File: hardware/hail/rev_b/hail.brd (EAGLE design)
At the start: 20.3 x 36.6 mm, 77 parts, among them J1 MICRO_USB_B_HIROSE_ZX62R-B-5P, J2 TC2030-JLINK-NL_NOSILK, J3 TC2030-JLINK-NL_NOSILK, U1 FT231XQ, U2 FXOS8700CQ, U3 ISL29035, U4 MAX8887EZK33+T, U5 NRF51822QF, U6 SAM4LC8BA, U7 SI7021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

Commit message: Hail rev B!
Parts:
- removed JP3: M12PTH-CST-L, Particle:1X12-CASTELLATED
- removed JP4: M12PTH-CST-R, Particle:1X12-CASTELLATED
- removed U$4: (no value), logos:HAIL
- added J4, J5: TC2030-JLINK-NL_NOSILK, connector:TC2030-IDC-NL_NOSILK
- J2: value TC2030-JLINK-NL_NOSILK -> M12PTH-CST-L; device connector:TC2030-IDC-NL_NOSILK -> Particle:1X12-CASTELLATED
- J3: value TC2030-JLINK-NL_NOSILK -> M12PTH-CST-R; device connector:TC2030-IDC-NL_NOSILK -> Particle:1X12-CASTELLATED
- R10: value 100k -> 10k
- R13: value 1k -> 100k
- R6: value 10k -> 1k
- U$3: device logos:UMICH_SOLID_75MIL -> logos:LAB11_SOLID_80MIL
- moved R12 23.6 mm to (7.72, 10.9), turned to 90 degrees
- moved J3 18.2 mm to (19.1, 18.3), flipped to the top, turned to 0 degrees
- moved R10 14.6 mm to (13.3, 24.0), turned to 270 degrees
- moved R9 13.2 mm to (4.50, 14.2), turned to 0 degrees
- moved J2 11.8 mm to (1.27, 18.3), turned to 180 degrees
- moved R8 11.8 mm to (2.79, 25.9)
- moved R6 11.0 mm to (10.2, 25.6), turned to 0 degrees
- moved R13 9.71 mm to (16.8, 32.8), turned to 270 degrees
- moved R7 9.33 mm to (3.81, 16.6), turned to 90 degrees
- moved R11 1.02 mm to (6.71, 10.9)
- moved U$3 0.41 mm to (8.13, 23.1)
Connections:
- net !LIGHT_INT: now also R9.1; no longer R8.1
- net !NRF_RESET: now also J5.2; no longer J3.2
- net !SAM4L_RESET: now also J3.11, J4.3, R6.2; no longer J2.3, JP4.11, R13.2
- net 5V: now also J2.1; no longer JP3.1
- net BUCK/LDO_N1: now also R10.2; no longer R9.2
- net BUTTON: now also R13.1; no longer R12.1
- net GND: now also J2.2, J3.9, J4.5, J5.5, R10.1; no longer J2.5, J3.5, JP3.2, JP4.9, R9.1
- net N$24: now also R6.1; no longer R13.1
- net N$6: now also J5.4; no longer J3.4
- net PARTICLE_A0: now also J2.12; no longer JP3.12
- net PARTICLE_A1: now also J2.11; no longer JP3.11
- net PARTICLE_A2: now also J2.10; no longer JP3.10
- net PARTICLE_A3: now also J2.9; no longer JP3.9
- net PARTICLE_A4: now also J2.8; no longer JP3.8
- net PARTICLE_A5: now also J2.7; no longer JP3.7
- net PARTICLE_D0: now also J3.1; no longer JP4.1
- net PARTICLE_D1: now also J3.2; no longer JP4.2
- net PARTICLE_D2: now also J3.3; no longer JP4.3
- net PARTICLE_D3: now also J3.4; no longer JP4.4
- net PARTICLE_D4: now also J3.5; no longer JP4.5
- net PARTICLE_D5: now also J3.6; no longer JP4.6
- net PARTICLE_D6: now also J3.7; no longer JP4.7
- net PARTICLE_D7: now also J3.8; no longer JP4.8
- net PARTICLE_DAC: now also J2.6; no longer JP3.6
- net PARTICLE_RX: now also J2.4; no longer JP3.4
- net PARTICLE_TX: now also J2.3; no longer JP3.3
- net PARTICLE_WKP: now also J2.5; no longer JP3.5
- net SAM4L_SWDCLK: now also J4.4, R12.1; no longer J2.4, R11.1
- net SAM4L_SWDIO: now also J4.2, R11.1; no longer J2.2, R10.1
- net SENSORS_SCL: now also R8.1; no longer R7.1
- net SENSORS_SDA: now also R7.1; no longer R6.1
- net VCC: now also J3.12, J4.1, J5.1, R13.2, R9.2; no longer J2.1, J3.1, JP4.12, R10.2, R6.2
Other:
- board text added: "03-2017"
- board text removed: "01-2017"
- board text removed: "A"

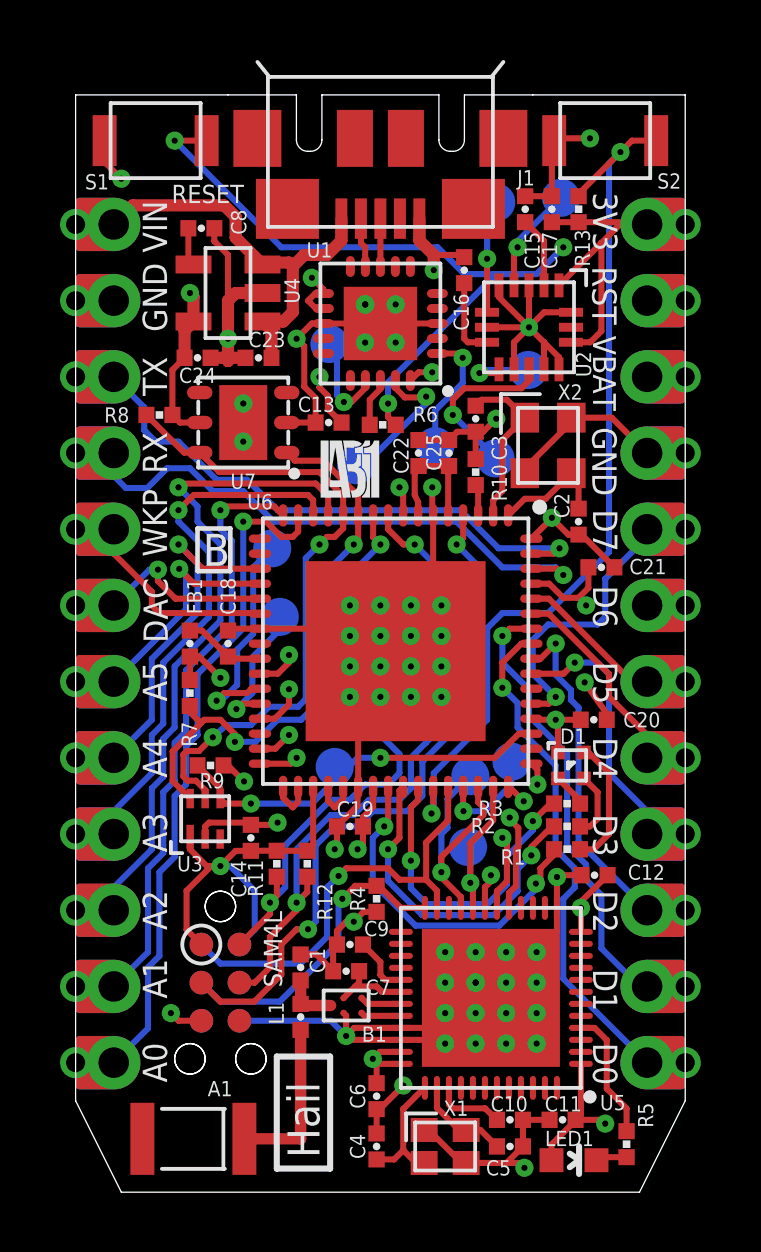
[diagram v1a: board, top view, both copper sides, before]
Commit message: update layout for MacroFab Standard 4 Layer DRU
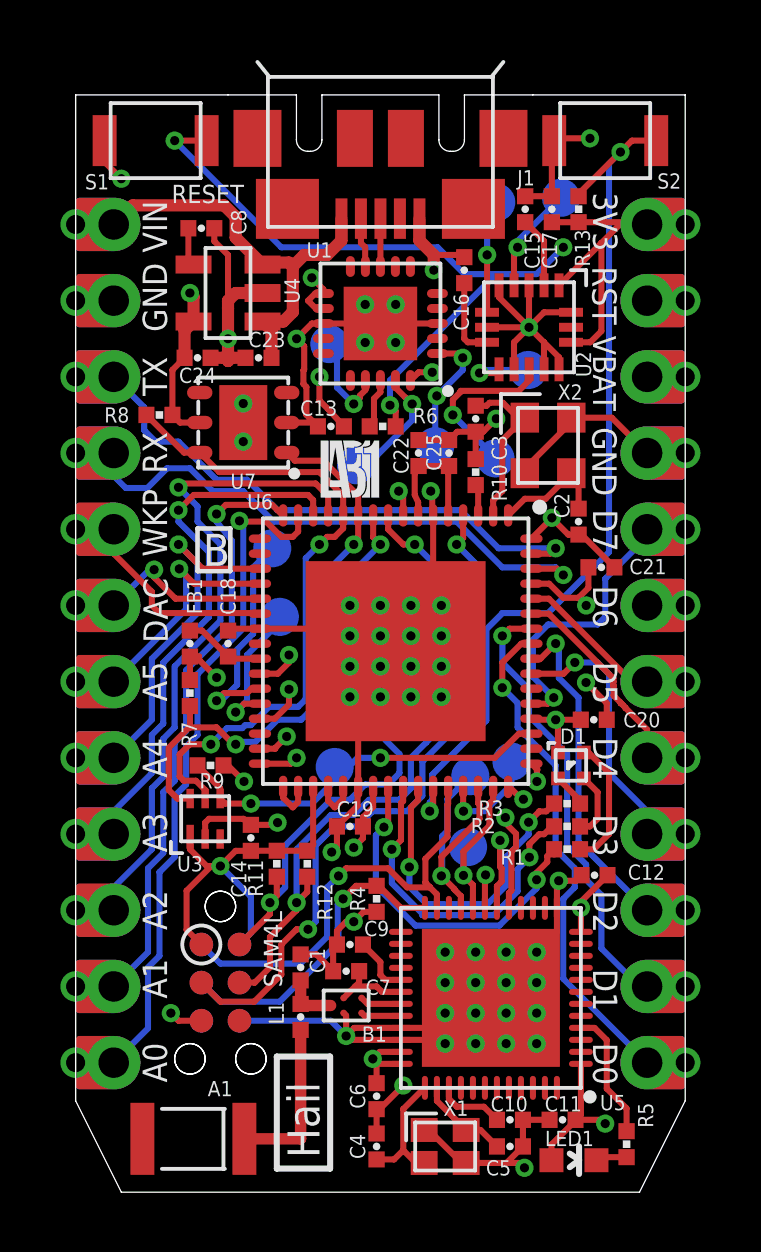
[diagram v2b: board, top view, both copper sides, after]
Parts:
- moved C13 0.15 mm to (8.51, 25.5)
- moved R6 0.05 mm to (10.2, 25.5)
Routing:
- net FTDI_IN: track 23.6 -> 21.9 mm, vias 2 -> 3
- net PARTICLE_D4: track 6.74 -> 7.50 mm
- net !FTDI_RTS: track 17.6 -> 17.0 mm
- net SENSORS_SDA: track 36.7 -> 37.2 mm
- net GND: track 107.8 -> 108.2 mm, vias 58 -> 56
